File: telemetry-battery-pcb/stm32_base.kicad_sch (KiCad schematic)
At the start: 41 parts, among them J1 Network Connector, J2 STDC14, SW1 SW_Push, U1 LD39050PU33R, U2 STM32G474RBT6, U3 SN65HVD230, Y1 8MHz

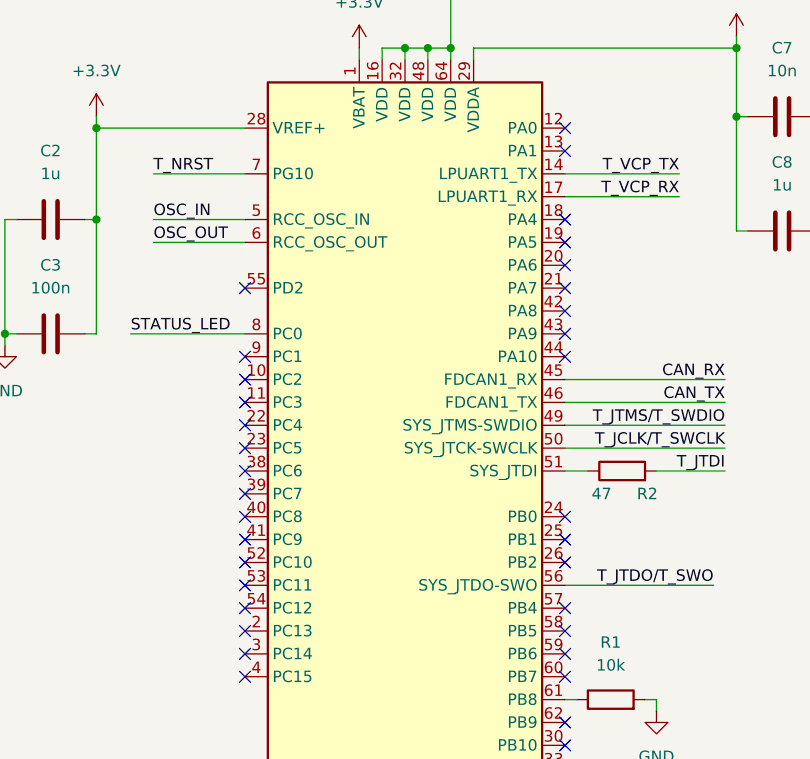
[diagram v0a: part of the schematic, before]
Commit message: telemetry-battery-pcb: add LTC2944
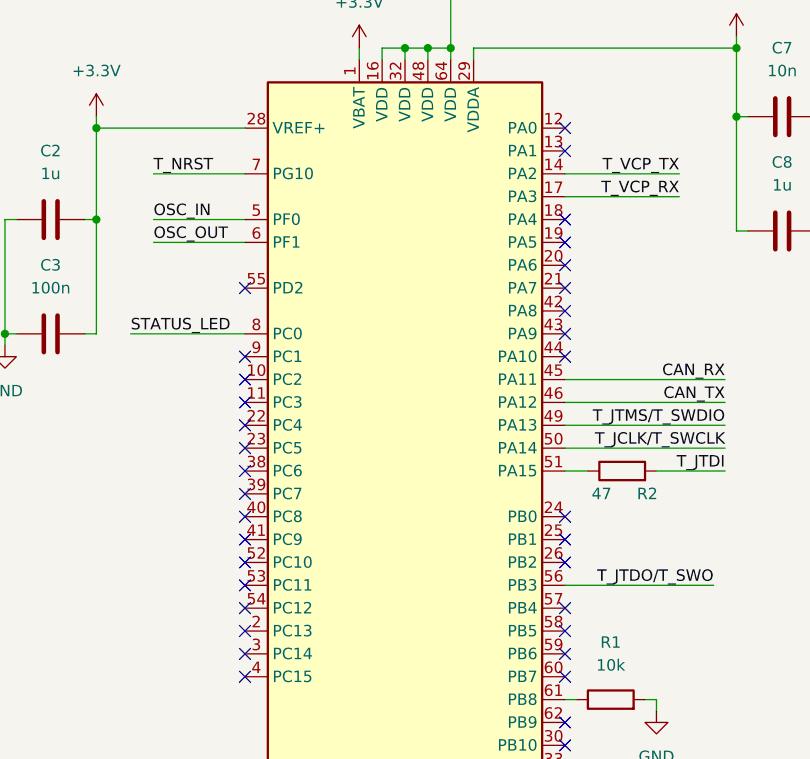
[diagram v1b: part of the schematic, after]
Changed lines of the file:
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@@
 		)
 		(pin "45"
-			(alternate "FDCAN1_RX")
 		)
 		(pin "27"
 		)
 		(pin "56"
-			(alternate "SYS_JTDO-SWO")
 		)
 		(pin "23"
@@
 		)
 		(pin "17"
-			(alternate "LPUART1_RX")
 		)
 		(pin "36"
@@
 		)
 		(pin "14"
-			(alternate "LPUART1_TX")
 		)
 		(pin "54"
@@
 		)
 		(pin "46"
-			(alternate "FDCAN1_TX")
 		)
 		(pin "43"
@@
 		)
 		(pin "49"
-			(alternate "SYS_JTMS-SWDIO")
 		)
 		(pin "20"
@@
 		)
 		(pin "6"
-			(alternate "RCC_OSC_OUT")
 		)
 		(pin "28"
@@
 		)
 		(pin "51"
-			(alternate "SYS_JTDI")
 		)
 		(pin "53"
@@
 		)
 		(pin "50"
-			(alternate "SYS_JTCK-SWCLK")
 		)
 		(pin "10"
@@
 		)
 		(pin "5"
-			(alternate "RCC_OSC_IN")
 		)
 		(pin "11"
@@
 			)
 		)
-		(property "Datasheet" "https://www.keyelco.com/userAssets/file/M65p56.pdf"
+		(property "Datasheet" "~"
 			(at 185.42 85.09 0)
 			(effects
@@
 			)
 		)
-		(property "Datasheet" "https://www.keyelco.com/userAssets/file/M65p56.pdf"
+		(property "Datasheet" "~"
 			(at 205.74 83.82 0)
 			(effects
@@
 			)
 		)
-		(property "Datasheet" "https://www.keyelco.com/userAssets/file/M65p56.pdf"
+		(property "Datasheet" "~"
 			(at 191.77 83.82 0)
 			(effects
@@
 			)
 		)
-		(property "Datasheet" "https://www.keyelco.com/userAssets/file/M65p56.pdf"
+		(property "Datasheet" "~"
 			(at 199.39 71.12 0)
 			(effects
@@
 			)
 		)
-		(property "Datasheet" "https://www.keyelco.com/userAssets/file/M65p56.pdf"
+		(property "Datasheet" "~"
 			(at 181.61 71.12 0)
 			(effects
